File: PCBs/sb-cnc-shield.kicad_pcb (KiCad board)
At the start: 2 copper layers, 69.1 x 76.3 mm, 31 parts, among them P10 power switch, P8 12V-36V, Q0 IRF630, SW1 RESET, U1 ARDUINO_UNO_SHIELD/hi five re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, U2 X, U3 Y, U4 Z, U5 A

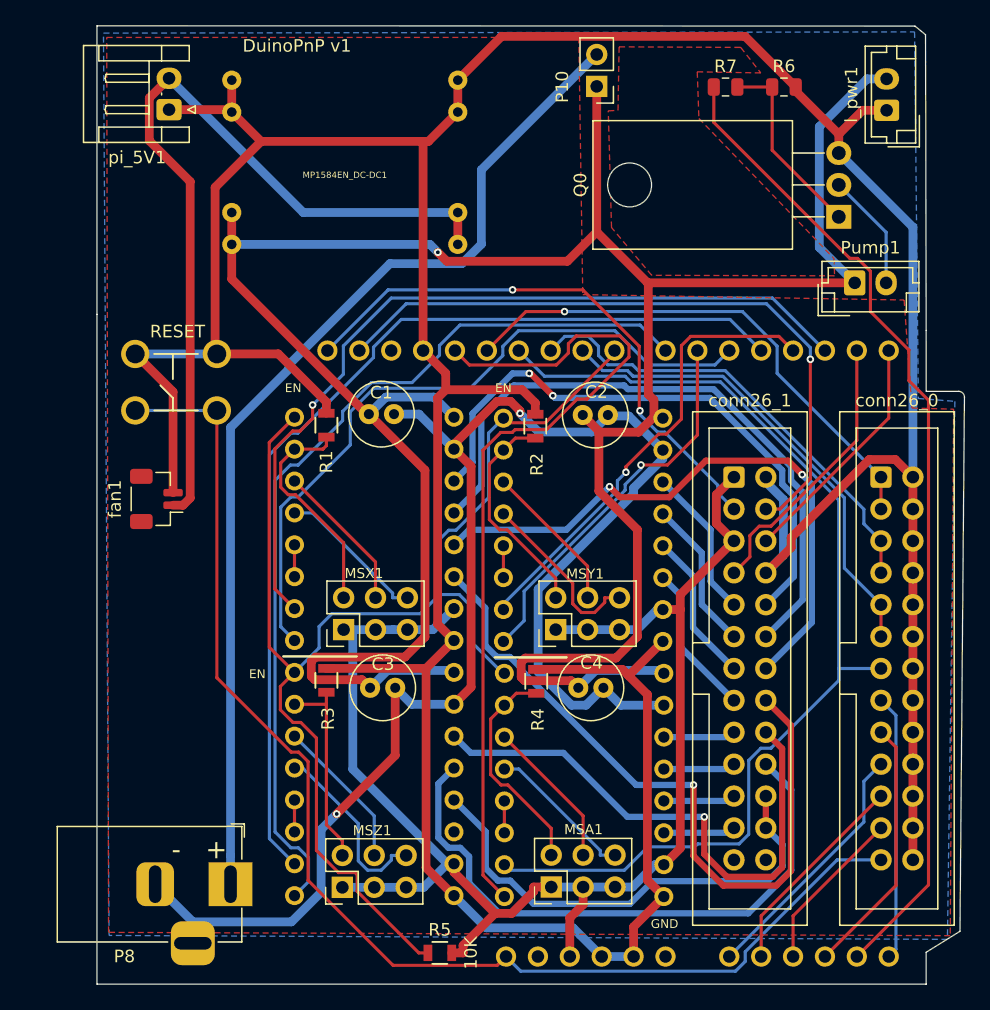
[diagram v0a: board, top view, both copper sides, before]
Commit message: correct z1A pinoutgit add .!
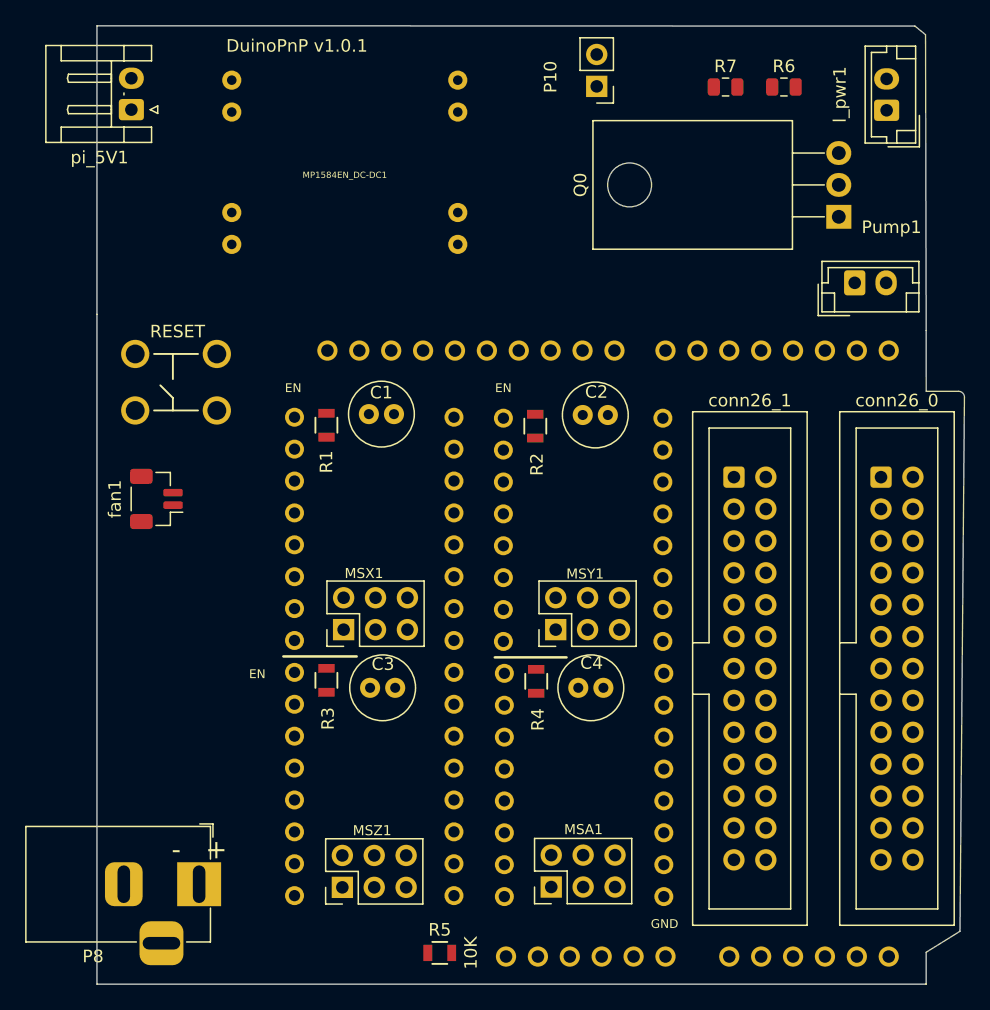
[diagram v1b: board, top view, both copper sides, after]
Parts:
- moved pi_5V1 3.00 mm to (117.0, 49.7)
- moved P8 2.50 mm to (122.4, 111.4)
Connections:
- conn26_1 pad 24: z1A -> z1B
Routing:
- net GND: track 336.0 -> 0.00 mm
- net VIN: track 216.3 -> 0.00 mm, vias 1 -> 0
- net GNDA: track 123.8 -> 0.00 mm, vias 2 -> 0
- net +5V: track 117.5 -> 0.00 mm
- net EN: track 103.8 -> 0.00 mm
- net RESET: track 100.6 -> 0.00 mm
- net SPIN_EN: track 84.7 -> 0.00 mm
- net VIN_: track 81.5 -> 0.00 mm
- net pump_ctrl: track 79.1 -> 0.00 mm
- net ZSTEP: track 78.5 -> 0.00 mm
- net ZDIR: track 72.9 -> 0.00 mm
- net SPIN_DIR: track 67.9 -> 0.00 mm
- net 5V_pi: track 67.0 -> 0.00 mm
- net XSTEP: track 65.8 -> 0.00 mm, vias 1 -> 0
- net x1B: track 57.1 -> 0.00 mm, vias 1 -> 0
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- removed copper zone on F.Cu, net (none)
- removed copper zone on B.Cu, net GND
- removed copper zone on F.Cu, net VIN
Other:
- board text added: "DuinoPnP v1.0.1"
- board text removed: "DuinoPnP v1"

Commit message: add DB25 pinout
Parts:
- removed fan1: fan5V, Connector_JST:JST_SH_BM02B-SRSS-TB_1x02-1MP_P1.00mm_Vertical
- added Pled1: yellow, LED_THT:LED_D3.0mm_Horizontal_O1.27mm_Z2.0mm, F.Cu at (116.7, 75.0)
- added Rp1: Rp, Resistor_SMD:R_0805_2012Metric, F.Cu at (155.1, 63.3)
- added Rpwr1: Rpwr, Resistor_SMD:R_0805_2012Metric, F.Cu at (148.2, 58.1)
- added Rpwr_1: Rpwr_, Resistor_SMD:R_0805_2012Metric, F.Cu at (121.6, 102.7)
- added Rstp1: RstpA, Resistor_SMD:R_0805_2012Metric, F.Cu at (125.8, 67.5)
- added RstpX1: RstpX, Resistor_SMD:R_0805_2012Metric, F.Cu at (148.2, 53.1)
- added RstpY1: RstpY, Resistor_SMD:R_0805_2012Metric, F.Cu at (148.2, 63.3)
- added RstpZ1: RstpZ, Resistor_SMD:R_0805_2012Metric, F.Cu at (126.0, 73.1)
- added V_led1: red, LED_THT:LED_D3.0mm_Horizontal_O1.27mm_Z2.0mm, F.Cu at (116.3, 100.0)
- added Vled1: green, LED_THT:LED_D3.0mm_Horizontal_O1.27mm_Z2.0mm, F.Cu at (116.3, 95.0)
- added ledA1: blue, LED_THT:LED_D3.0mm_Horizontal_O1.27mm_Z2.0mm, F.Cu at (116.7, 70.0)
- added ledX1: blue, LED_THT:LED_D3.0mm_Horizontal_O1.27mm_Z2.0mm, F.Cu at (116.7, 55.0)
- added ledY1: blue, LED_THT:LED_D3.0mm_Horizontal_O1.27mm_Z2.0mm, F.Cu at (116.7, 60.0)
- added ledZ1: white, LED_THT:LED_D3.0mm_Horizontal_O1.27mm_Z2.0mm, F.Cu at (116.7, 65.0)
- moved SW1 16.6 mm to (118.3, 90.2)
- moved pi_5V1 0.27 mm to (117.0, 50.0)
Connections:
- net /D renamed D

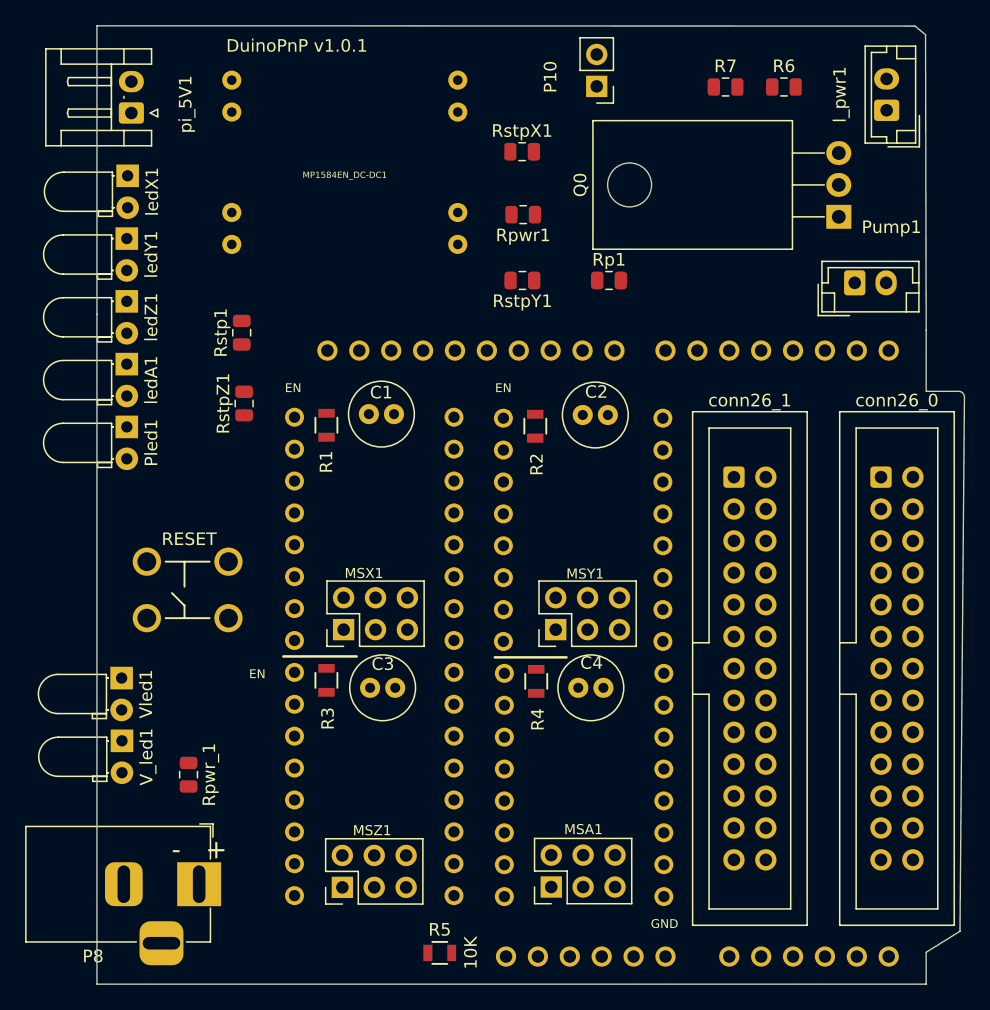
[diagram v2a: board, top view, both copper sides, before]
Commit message: pinout modify
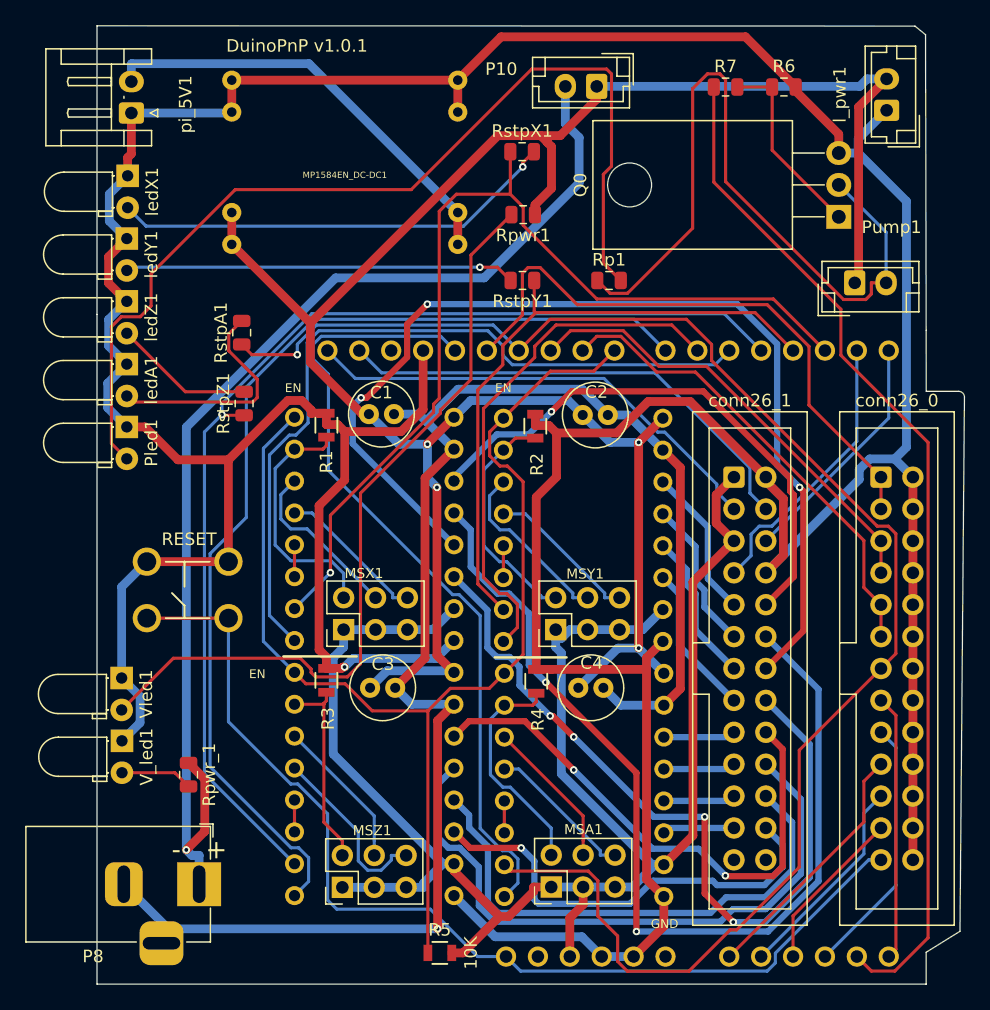
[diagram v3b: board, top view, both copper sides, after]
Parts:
- P10: footprint Connector_PinHeader_2.54mm:PinHeader_1x02_P2.54mm_Vertical -> Connector_JST:JST_EH_B2B-EH-A_1x02_P2.50mm_Vertical
- renumbered Rstp1 to RstpA1
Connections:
- net SPIN_DIR renamed ADIR
- net SPIN_EN renamed ASTEP
- Rpwr1 pad 1: Vin -> VIN
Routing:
- net GND: track 0.00 -> 376.3 mm, vias 0 -> 1
- net VIN: track 0.00 -> 179.6 mm, vias 0 -> 4
- net +5V: track 0.00 -> 139.5 mm
- net GNDA: track 0.00 -> 127.2 mm, vias 0 -> 1
- net ASTEP: track 0.00 -> 126.6 mm, vias 0 -> 1
- net EN: track 0.00 -> 94.8 mm
- net VIN_: track 0.00 -> 92.7 mm, vias 0 -> 1
- net ZSTEP: track 0.00 -> 89.1 mm, vias 0 -> 1
- net RESET: track 0.00 -> 83.1 mm
- net ZDIR: track 0.00 -> 82.4 mm
- net x1A: track 0.00 -> 82.3 mm, vias 0 -> 3
- net pump_ctrl: track 0.00 -> 82.1 mm
- net Net-(Pled1-Pad2): track 0.00 -> 78.3 mm
- net x2A: track 0.00 -> 77.3 mm, vias 0 -> 2
- net XSTEP: track 0.00 -> 77.1 mm, vias 0 -> 1
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
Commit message: update
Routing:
- added copper zone on F.Cu, net GND
- added copper zone on B.Cu, net VIN
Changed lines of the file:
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@@
   (general
     (thickness 1.6)
-    (drawings 32)
+    (drawings 33)
     (tracks 757)
     (zones 0)
@@
       (drillshape 0)
       (scaleselection 1)
-      (outputdirectory "../gerbers/"))
+      (outputdirectory "gerbers/"))
   )
   (net 0 "")
@@
     )
   )
+  (dimension 2 (width 0.15) (layer Dwgs.User)
+    (gr_text "2,000 mm" (at 102.95 58.75 270) (layer Dwgs.User)
+      (effects (font (size 1 1) (thickness 0.15)))
+    )
+    (feature1 (pts (xy 112.5 59.75) (xy 103.663579 59.75)))
+    (feature2 (pts (xy 112.5 57.75) (xy 103.663579 57.75)))
+    (crossbar (pts (xy 104.25 57.75) (xy 104.25 59.75)))
+    (arrow1a (pts (xy 104.25 59.75) (xy 103.663579 58.623496)))
+    (arrow1b (pts (xy 104.25 59.75) (xy 104.836421 58.623496)))
+    (arrow2a (pts (xy 104.25 57.75) (xy 103.663579 58.876504)))
+    (arrow2b (pts (xy 104.25 57.75) (xy 104.836421 58.876504)))
+  )
   (dimension 2.418213 (width 0.15) (layer Dwgs.User)
     (gr_text "2,418 mm" (at 120.843128 124.024887 0.6018242894) (layer Dwgs.User)
@@
   (segment (start 121.595 103.6345) (end 120.5005 102.54) (width 0.25) (layer F.Cu) (net 72))
   (segment (start 120.5005 102.54) (end 116.291 102.54) (width 0.25) (layer F.Cu) (net 72))
+  (zone (net 7) (net_name GND) (layer F.Cu) (hatch edge 0.508)
+    (connect_pads (clearance 0.508))
+    (min_thickness 0.254)
+    (fill yes (arc_segments 32) (thermal_gap 0.508) (thermal_bridge_width 0.508))
+    (polygon
+      (pts
+        (xy 180.25 43.75) (xy 180.25 72.25) (xy 183 72.25) (xy 182.75 115) (xy 180 116.75)
+        (xy 180 119.25) (xy 114.5 119.25) (xy 114.25 43) (xy 179.25 43)
+      )
+    )
+  )
+  (zone (net 11) (net_name VIN) (layer B.Cu) (hatch edge 0.508)
+    (connect_pads (clearance 0.508))
+    (min_thickness 0.254)
+    (fill yes (arc_segments 32) (thermal_gap 0.508) (thermal_bridge_width 0.508))
+    (polygon
+      (pts
+        (xy 180.25 44) (xy 180 72.5) (xy 182.25 72.5) (xy 183 73) (xy 182.75 115)
+        (xy 180 116.75) (xy 180 119) (xy 114.5 119) (xy 114.25 43.25) (xy 179.25 43.25)
+      )
+    )
+  )
 )
